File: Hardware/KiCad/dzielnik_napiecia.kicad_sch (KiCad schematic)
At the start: 2 parts

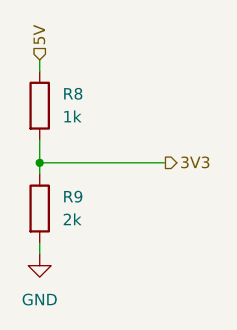
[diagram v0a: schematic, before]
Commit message: change to pinout of atemega for PWM Motor 1
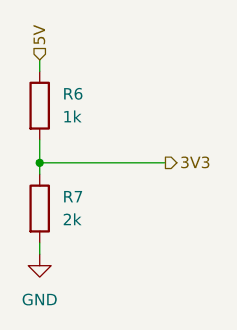
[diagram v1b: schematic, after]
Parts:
- renumbered R8 to R6, R9 to R7
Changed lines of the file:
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@@
 (kicad_sch
-	(version 20231120)
+	(version 20250114)
 	(generator "eeschema")
-	(generator_version "8.0")
+	(generator_version "9.0")
 	(paper "A4")
 	(junction
@@
 		(shape input)
 		(at 106.68 29.21 90)
-		(fields_autoplaced yes)
 		(effects
 			(font
@@
 		(shape output)
 		(at 120.65 40.64 0)
-		(fields_autoplaced yes)
 		(effects
 			(font
@@
 		(dnp no)
 		(fields_autoplaced yes)
-		(property "Reference" "#PWR044"
+		(property "Reference" "#PWR043"
 			(at 106.68 57.15 0)
 			(effects
@@
 		(dnp no)
 		(fields_autoplaced yes)
-		(property "Reference" "R8"
+		(property "Reference" "R6"
 			(at 109.22 33.0199 0)
 			(effects
@@
 		(dnp no)
 		(fields_autoplaced yes)
-		(property "Reference" "R9"
+		(property "Reference" "R7"
 			(at 109.22 44.4499 0)
 			(effects
